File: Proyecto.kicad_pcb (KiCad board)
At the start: 2 copper layers, 42 parts, among them IC1 ATMEGA328P-A, P1 CONN_01X03, P2 CONN_01X03, Q1 BC808-40, Q2 BC808-40, SW1 SW_PUSH, U2 MCP2551-I/SN, U3 AMS1117, U4 ACS712, U5 ACS712

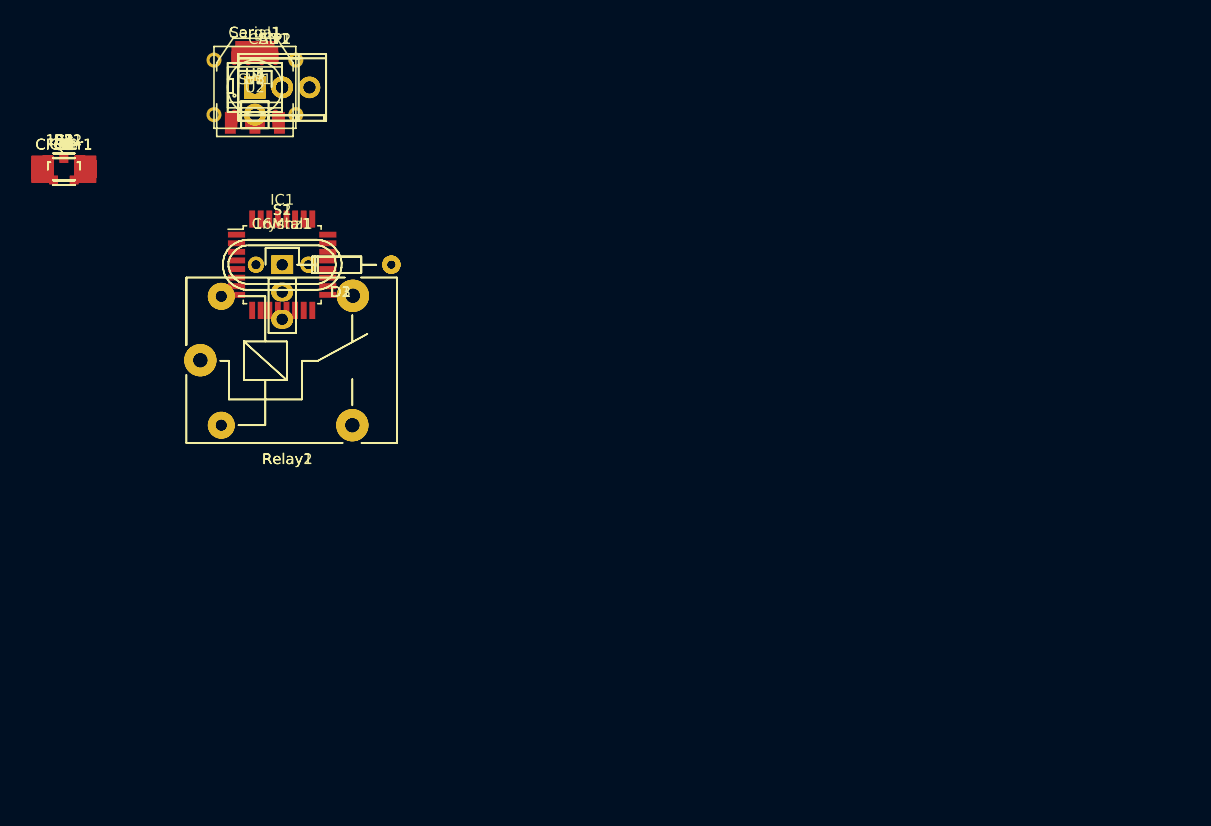
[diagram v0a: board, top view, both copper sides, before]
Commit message: fix
se quito el micro y se coloco pines hembra para insertar NanoArduino en
placa
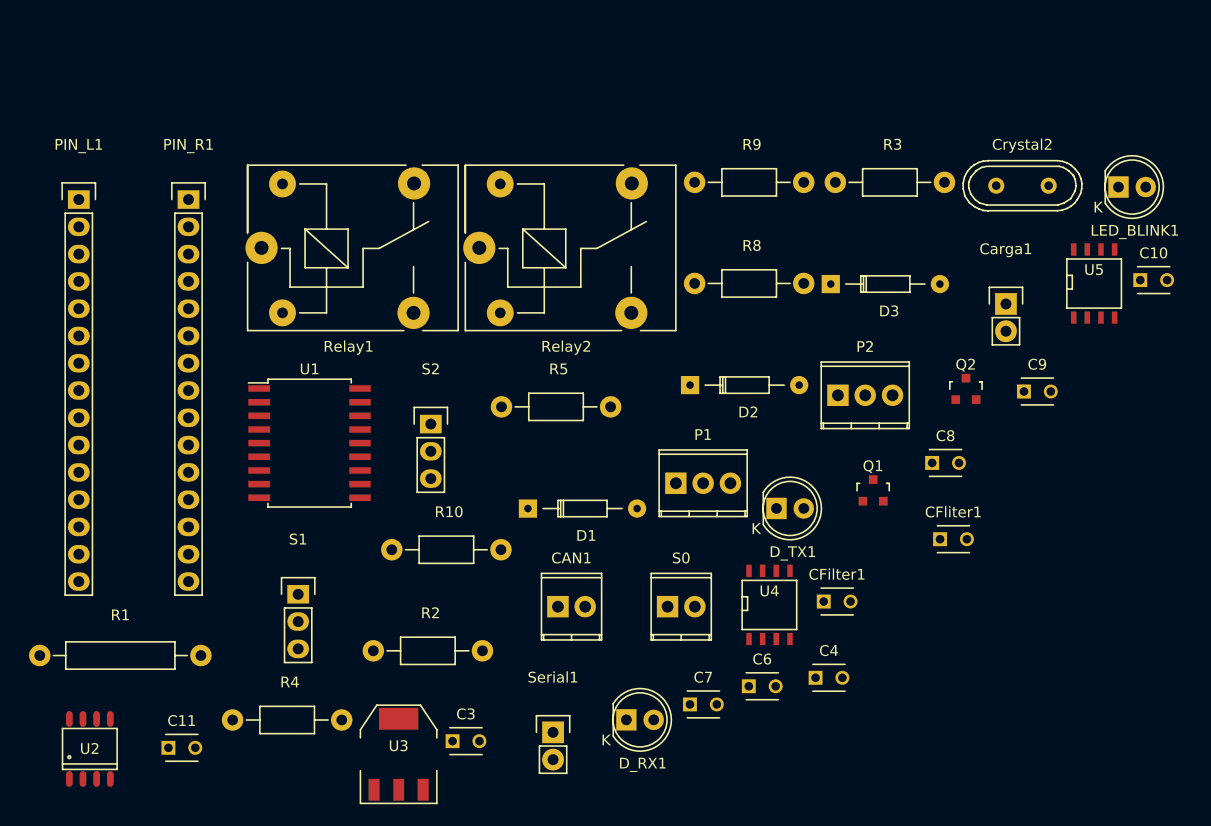
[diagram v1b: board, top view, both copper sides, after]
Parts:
- removed 10k1, 10k2: R, Resistors_SMD:R_1210
- removed 16Mhz1: Crystal, Crystals:Crystal_HC49-U_Vertical
- removed C1, C2: 22pf, Capacitors_SMD:C_1210
- removed C5: 100nf, Capacitors_SMD:C_1206_HandSoldering
- removed Crystal1: 16mhz, Crystals:Crystal_HC49-U_Vertical
- removed IC1: ATMEGA328P-A, Housings_QFP:TQFP-32_7x7mm_Pitch0.8mm
- removed SW1: SW_PUSH, Buttons_Switches_ThroughHole:SW_PUSH_SMALL
- added Crystal2: 16Mhz, Crystals:Crystal_HC49-U_Vertical, F.Cu at (193.3, 65.9)
- added D_RX1: LED, LEDs:LED-5MM, F.Cu at (156.4, 115.6)
- added D_TX1: LED, LEDs:LED-5MM, F.Cu at (170.4, 95.9)
- added LED_BLINK1: LED, LEDs:LED-5MM, F.Cu at (202.2, 66.0)
- added PIN_L1: CONN_01X15, Pin_Headers:Pin_Header_Straight_1x15, F.Cu at (105.4, 67.2)
- added PIN_R1: CONN_01X15, Pin_Headers:Pin_Header_Straight_1x15, F.Cu at (115.6, 67.2)
- added R10: 1k, Resistors_ThroughHole:Resistor_Horizontal_RM10mm, F.Cu at (134.6, 99.8)
- added R5: 120, Resistors_ThroughHole:Resistor_Horizontal_RM10mm, F.Cu at (144.8, 86.5)
- added R8: 1k, Resistors_ThroughHole:Resistor_Horizontal_RM10mm, F.Cu at (162.8, 75.0)
- added R9: 1k, Resistors_ThroughHole:Resistor_Horizontal_RM10mm, F.Cu at (162.8, 65.6)
- added U1: MCP2515, Housings_SOIC:SOIC-18_7.5x11.6mm_Pitch1.27mm, F.Cu at (126.9, 89.9)
- C10, C11, C3, C4, C6, C7, C8, C9: footprint Capacitors_SMD:C_1206_HandSoldering -> Capacitors_ThroughHole:C_Disc_D3_P2.5
- CFilter1, CFliter1: footprint Capacitors_SMD:C_1206 -> Capacitors_ThroughHole:C_Disc_D3_P2.5
- R1: value R -> 10k; footprint Resistors_SMD:R_1206_HandSoldering -> Resistors_ThroughHole:Resistor_Horizontal_RM15mm
- R2: value R -> 10k; footprint Resistors_SMD:R_1210_HandSoldering -> Resistors_ThroughHole:Resistor_Horizontal_RM10mm
- R3: value R -> 1k; footprint Resistors_SMD:R_1210_HandSoldering -> Resistors_ThroughHole:Resistor_Horizontal_RM10mm
- R4: value 120 -> 1k; footprint Resistors_SMD:R_1210_HandSoldering -> Resistors_ThroughHole:Resistor_Horizontal_RM10mm
- moved C10 100.7 mm to (204.3, 74.7)
- moved C9 91.7 mm to (193.4, 85.1)
- moved CFliter1 88.5 mm to (185.6, 98.8)
- moved Q2 86.4 mm to (188.0, 84.8)
- moved C8 85.3 mm to (184.9, 91.7)
- moved C4 84.5 mm to (174.0, 111.7)
- moved CFilter1 81.4 mm to (174.8, 104.6)
- moved Q1 81.0 mm to (179.4, 94.3)
- moved U5 80.2 mm to (200.0, 75.0)
- moved C6 79.9 mm to (167.8, 112.5)
- moved C7 76.7 mm to (162.3, 114.2)
- moved Carga1 72.8 mm to (191.7, 76.9)
- moved R3 71.8 mm to (175.9, 65.6)
- moved U4 67.9 mm to (169.7, 104.9)
- moved Serial1 66.1 mm to (149.6, 116.8)
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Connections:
- R1 pad 2: RESET -> Net-(R1-Pad2)
- R2 pad 1: Net-(Q1-Pad1) -> +5V
- R2 pad 2: Net-(IC1-Pad11) -> /CS
- R3 pad 1: Net-(Q2-Pad1) -> Net-(Q1-Pad1)
- R3 pad 2: Net-(IC1-Pad10) -> /R2
- R4 pad 1: Net-(CAN1-Pad2) -> Net-(Q2-Pad1)
- R4 pad 2: Net-(Carga1-Pad1) -> /R1
- U4 pad 1: Net-(P1-Pad3) -> Net-(Relay1-Pad1)
- U4 pad 2: Net-(P1-Pad3) -> Net-(Relay1-Pad1)
- U4 pad 3: Net-(Relay1-Pad1) -> Net-(P1-Pad3)
- U4 pad 4: Net-(Relay1-Pad1) -> Net-(P1-Pad3)
- U4 pad 7: AC1 -> /AC1
- U5 pad 7: AC2 -> /AC2
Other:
- rule pad_to_mask_clearance: 0.2 -> 0

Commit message: fix pcb
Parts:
- moved CAN1 74.5 mm to (85.1, 68.6)
- moved U4 65.7 mm to (147.3, 43.2)
- moved U5 52.7 mm to (147.3, 72.4), turned to 180 degrees
- moved D_TX1 52.1 mm to (208.5, 131.5)
- moved Q1 52.1 mm to (217.5, 129.8)
- moved C8 52.1 mm to (223.0, 127.3)
- moved CFliter1 52.1 mm to (223.7, 134.4)
- moved Carga1 52.1 mm to (229.8, 112.5)
- moved Crystal2 52.1 mm to (231.4, 101.5)
- moved D3 52.1 mm to (213.5, 110.6)
- moved R3 52.1 mm to (214.0, 101.1)
- moved C9 52.1 mm to (231.5, 120.6)
- moved CFilter1 52.1 mm to (212.9, 140.2)
- moved Q2 52.1 mm to (226.1, 120.4)
- moved P1 47.9 mm to (162.6, 45.7), turned to 270 degrees
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
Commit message: fix terrena
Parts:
- added D4: LED 2, LEDs:LED-5MM, B.Cu at (122.9, 108.7)
- added R11: 1k, Resistors_ThroughHole:Resistor_Horizontal_RM10mm, B.Cu at (117.3, 108.7)
- C10, C11, C4, C8, C9, CAN1, CFilter1, CFliter1, Carga1, Crystal2, D1, D2, D3, D_RX1, D_TX1, LED_BLINK1, P1, P2, R10, R2, R3, R4, R5, R8, R9, Relay1, Relay2, S0: moved to B.Cu
- R1: footprint Resistors_ThroughHole:Resistor_Horizontal_RM15mm -> Resistors_ThroughHole:Resistor_Horizontal_RM10mm; moved to B.Cu
- U2: footprint Power_Integrations:SO-8 -> SMD_Packages:SOIC-8-N
- moved CFliter1 146.4 mm to (98.6, 58.4), turned to 180 degrees
- moved Q2 127.1 mm to (106.2, 78.5), turned to 180 degrees
- moved CFilter1 125.6 mm to (93.5, 101.1), turned to 180 degrees
- moved Q1 116.3 mm to (106.2, 96.3), turned to 90 degrees
- moved C10 116.0 mm to (89.4, 58.4)
- moved D3 113.1 mm to (106.2, 74.9), turned to 90 degrees
- moved R3 99.9 mm to (114.3, 94.0), turned to 90 degrees
- moved P1 95.5 mm to (78.2, 90.6), turned to 90 degrees
- moved CAN1 90.0 mm to (164.3, 111.3)
- moved P2 85.2 mm to (78.2, 74.0), turned to 90 degrees
- moved U2 82.1 mm to (165.2, 98.3), turned to 180 degrees
- moved C8 82.0 mm to (172.7, 62.5)
- moved U1 82.0 mm to (157.2, 66.5), turned to 180 degrees
- moved C9 78.9 mm to (172.7, 68.1)
- moved U4 74.4 mm to (93.5, 94.5), turned to 180 degrees
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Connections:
- LED_BLINK1 pad 2: /LED_BLINK -> /LED
- PIN_L1 pad 1: Net-(PIN_L1-Pad1) -> /SO
- PIN_L1 pad 11: Net-(PIN_L1-Pad11) -> /LED
- PIN_L1 pad 12: /INT -> GND
- PIN_L1 pad 13: /CS -> Net-(PIN_L1-Pad13)
- PIN_L1 pad 14: /SI -> /tx
- PIN_L1 pad 15: /SO -> /rx
- PIN_L1 pad 2: Net-(PIN_L1-Pad2) -> /SI
- PIN_L1 pad 3: Net-(PIN_L1-Pad3) -> /CS
- PIN_L1 pad 4: GND -> /INT
- PIN_L1 pad 5: /LED_BLINK -> Net-(PIN_L1-Pad5)
- PIN_R1 pad 12: Net-(PIN_R1-Pad12) -> +5V
- Relay1 pad 3: Net-(P1-Pad2) -> Net-(P1-Pad1)
- Relay1 pad 4: Net-(P1-Pad1) -> Net-(P1-Pad3)
- Relay2 pad 3: Net-(P2-Pad2) -> Net-(P2-Pad1)
- Relay2 pad 4: Net-(P2-Pad1) -> Net-(P2-Pad3)
- S1 pad 2: GND -> +5V
- S1 pad 3: +5V -> GND
- S2 pad 2: GND -> +5V
- S2 pad 3: +5V -> GND
- Serial1 pad 1: Net-(PIN_L1-Pad2) -> /rx
- Serial1 pad 2: Net-(PIN_L1-Pad1) -> /tx
- U2 pad 6: Net-(CAN1-Pad2) -> Net-(CAN1-Pad1)
- U2 pad 7: Net-(CAN1-Pad1) -> Net-(CAN1-Pad2)
- U3 pad 4: (no net) -> +5V
- U4 pad 3: Net-(P1-Pad3) -> Net-(P1-Pad2)
- U4 pad 4: Net-(P1-Pad3) -> Net-(P1-Pad2)
- U5 pad 1: Net-(P2-Pad3) -> Net-(P2-Pad2)
- U5 pad 2: Net-(P2-Pad3) -> Net-(P2-Pad2)
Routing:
- net GND: track 0.00 -> 271.6 mm
- net +5V: track 0.00 -> 207.0 mm
- net Net-(R9-Pad2): track 0.00 -> 64.0 mm
- net /SCK: track 0.00 -> 45.1 mm
- net /INT: track 0.00 -> 39.9 mm
- net Net-(R8-Pad2): track 0.00 -> 31.5 mm
- net Net-(C6-Pad1): track 0.00 -> 24.1 mm
- net Net-(CAN1-Pad1): track 0.00 -> 18.5 mm
- net /SO: track 0.00 -> 17.4 mm, vias 0 -> 2
- net pin23: track 0.00 -> 16.6 mm
- net Net-(P2-Pad2): track 0.00 -> 16.5 mm
- net Net-(P1-Pad2): track 0.00 -> 16.0 mm
- net /SI: track 0.00 -> 14.9 mm
- net /CS: track 0.00 -> 14.5 mm
- net Net-(LED_BLINK1-Pad1): track 0.00 -> 13.7 mm
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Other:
- board outline added: 102.6 x 58.9 mm
- net class Default: clearance 0.2 -> 0.3556; trace_width 0.25 -> 0.3048; via_dia 0.6 -> 1.2; via_drill 0.4 -> 0.8
- rule trace_clearance: 0.2 -> 0.3556
- rule trace_min: 0.2 -> 0.3048
- rule via_min_drill: 0.3 -> 0.8
- rule via_min_size: 0.4 -> 1.2

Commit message: fix
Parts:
- PIN_L1, PIN_R1, S1, S2: moved to B.Cu
- moved R1 116.1 mm to (34.6, 105.5)
- moved R2 116.1 mm to (30.5, 103.0)
- moved C4 111.7 mm to (61.6, 132.3)
- moved R8 110.3 mm to (58.6, 127.3)
- moved R9 110.3 mm to (58.6, 117.6)
- moved D_TX1 110.3 mm to (53.5, 127.0)
- moved Serial1 110.3 mm to (41.3, 140.0)
- moved U2 110.3 mm to (62.8, 139.2)
- moved R5 110.3 mm to (64.7, 146.6)
- moved CAN1 110.3 mm to (61.9, 152.1)
- moved Carga1 110.3 mm to (55.0, 142.0)
- moved D_RX1 110.3 mm to (53.5, 119.4)
- moved S0 110.3 mm to (53.5, 152.1)
- moved R10 109.1 mm to (56.3, 133.1), turned to 90 degrees
- moved LED_BLINK1 109.0 mm to (47.4, 132.3)
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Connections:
- PIN_L1 pad 12: GND -> Net-(PIN_L1-Pad12)
- Relay1 pad 2: +5V -> Net-(D2-Pad2)
- Relay1 pad 5: Net-(D2-Pad2) -> +5V
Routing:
- net GND: track 271.6 -> 0.00 mm
- net +5V: track 207.0 -> 3.06 mm
- net Net-(R9-Pad2): track 64.0 -> 1.52 mm
- net /INT: track 39.9 -> 7.81 mm
- net Net-(R8-Pad2): track 31.5 -> 0.00 mm
- net Net-(C6-Pad1): track 24.1 -> 0.36 mm
- net Net-(CAN1-Pad1): track 18.5 -> 0.00 mm
- net pin23: track 16.6 -> 0.00 mm
- net Net-(P2-Pad2): track 16.5 -> 0.00 mm
- net Net-(P1-Pad2): track 16.0 -> 0.00 mm
- net Net-(LED_BLINK1-Pad1): track 13.7 -> 0.00 mm
- net Net-(Q2-Pad1): track 12.9 -> 0.00 mm
- net Net-(C9-Pad1): track 12.5 -> 0.50 mm
- net /R2: track 11.2 -> 0.00 mm
- net pin24: track 11.1 -> 0.00 mm
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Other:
- board outline removed
- net class Default: clearance 0.3556 -> 0.55
- rule trace_clearance: 0.3556 -> 0.55

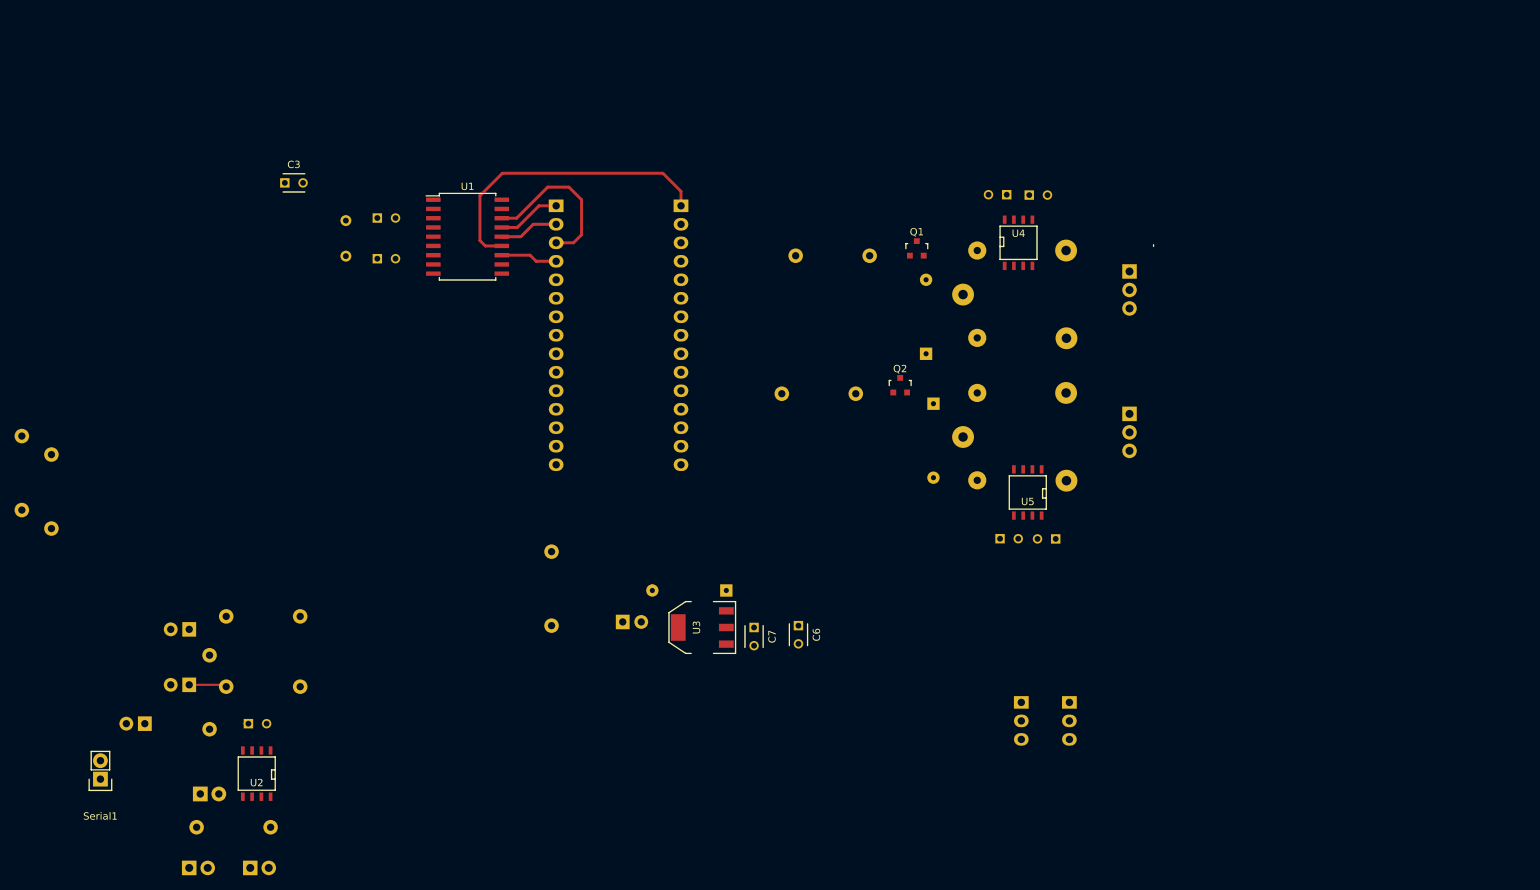
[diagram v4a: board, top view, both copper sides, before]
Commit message: fix casa
se dieron vuelta los pines del nano arudino
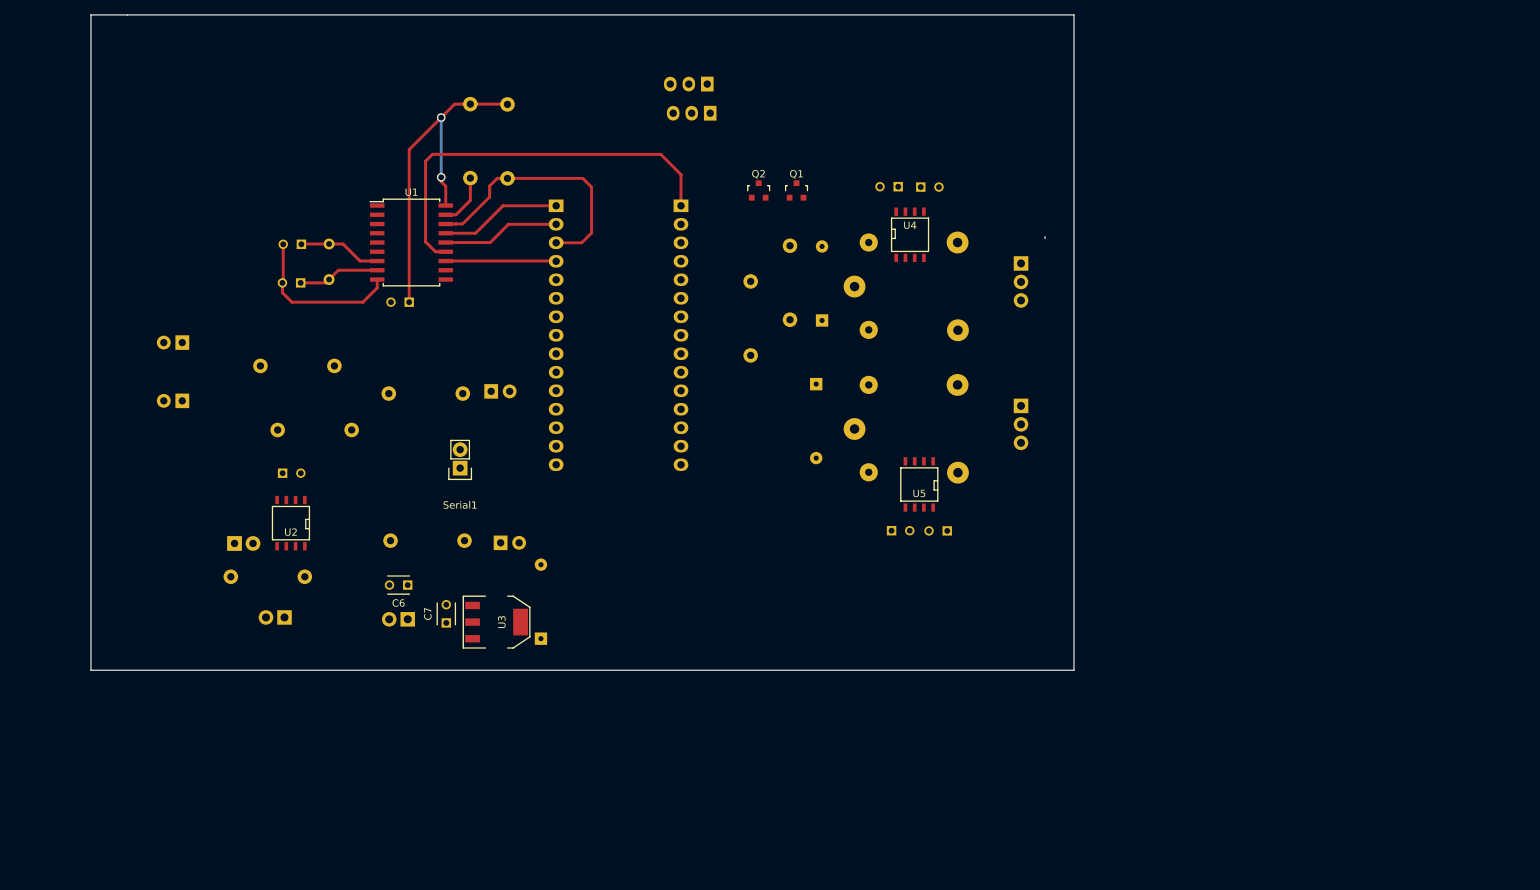
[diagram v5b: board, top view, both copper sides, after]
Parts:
- C3: moved to B.Cu
- moved S2 98.4 mm to (124.6, 44.5), turned to 90 degrees
- moved S1 91.5 mm to (125.0, 48.5), turned to 90 degrees
- moved R2 86.9 mm to (97.2, 47.3), turned to 270 degrees
- moved R1 81.9 mm to (92.1, 47.2), turned to 270 degrees
- moved LED_BLINK1 65.9 mm to (95.0, 86.7), turned to 0 degrees
- moved Serial1 65.3 mm to (90.7, 97.2)
- moved R10 57.7 mm to (91.1, 87.0), turned to 180 degrees
- moved C6 53.9 mm to (83.5, 113.3), turned to 180 degrees
- moved S0 45.5 mm to (83.5, 118.0), turned to 180 degrees
- moved C7 42.3 mm to (88.8, 118.5), turned to 90 degrees
- moved D_RX1 39.4 mm to (52.5, 80.0)
- moved D_TX1 39.0 mm to (52.5, 88.0)
- moved R8 36.0 mm to (65.6, 92.0)
- moved C4 34.7 mm to (66.3, 97.9)
- moved R9 34.7 mm to (63.3, 83.2)
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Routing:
- net (no net): track 0.00 -> 141.5 mm
- net +5V: track 3.06 -> 49.9 mm, vias 0 -> 2
- net GND: track 0.00 -> 22.2 mm
- net /CS: track 22.2 -> 37.1 mm
- net /SCK: track 41.4 -> 55.3 mm
- net Net-(C9-Pad1): track 0.50 -> 11.4 mm
- net Net-(C8-Pad1): track 0.64 -> 11.2 mm
- net /SI: track 8.17 -> 16.2 mm
- net /SO: track 8.70 -> 16.7 mm
- net /INT: track 7.81 -> 15.2 mm
- net Net-(R1-Pad2): track 0.00 -> 7.26 mm
- net Net-(D_TX1-Pad1): track 5.19 -> 0.00 mm
- net /LED: track 0.76 -> 0.00 mm
- net Net-(D3-Pad2): track 0.51 -> 0.00 mm
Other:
- board outline added: 135 x 90 mm

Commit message: fix terrena
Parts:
- removed D4: LED 2, LEDs:LED-5MM
- removed LED_BLINK1: LED, LEDs:LED-5MM
- removed Serial1: CONN_01X02, Pin_Headers:Pin_Header_Straight_1x02
- added ESP8266: CONN_02X04, Pin_Headers:Pin_Header_Straight_2x04, B.Cu at (112.9, 108.1)
- added LED1: LED, LEDs:LED-5MM, B.Cu at (90.8, 82.0)
- added LED_Gp1: LED, LEDs:LED-5MM, B.Cu at (105.7, 115.3)
- added LED_Gp2: LED, LEDs:LED-5MM, B.Cu at (112.4, 115.6)
- added LED_Vcc1: LED, LEDs:LED-5MM, B.Cu at (84.3, 97.0)
- added R12: 1k, Resistors_ThroughHole:Resistor_Horizontal_RM10mm, B.Cu at (104.1, 101.6)
- added R13: 2k2, Resistors_ThroughHole:Resistor_Horizontal_RM10mm, B.Cu at (118.4, 101.6)
- added R6: 1k, Resistors_ThroughHole:Resistor_Horizontal_RM10mm, B.Cu at (122.6, 115.6)
- added R7: 1k, Resistors_ThroughHole:Resistor_Horizontal_RM10mm, B.Cu at (127.0, 115.6)
- C6, C7: moved to B.Cu
- moved C10 97.4 mm to (63.9, 79.4), turned to 270 degrees
- moved C4 91.5 mm to (148.8, 58.4)
- moved C3 81.2 mm to (158.5, 106.2)
- moved C11 67.5 mm to (85.3, 74.7)
- moved D_TX1 41.0 mm to (78.3, 56.1), turned to 0 degrees
- moved R8 40.1 mm to (73.8, 52.7), turned to 270 degrees
- moved D_RX1 40.1 mm to (78.4, 49.4), turned to 0 degrees
- moved R9 33.7 mm to (67.6, 49.8), turned to 270 degrees
- moved R5 23.5 mm to (65.8, 88.9), turned to 0 degrees
- moved U2 22.7 mm to (69.8, 82.3)
- moved CAN1 22.1 mm to (64.6, 95.8), turned to 90 degrees
- moved S0 20.7 mm to (65.5, 107.7), turned to 90 degrees
- moved C7 19.4 mm to (74.7, 105.2)
- moved U3 19.4 mm to (81.6, 105.1)
- moved D1 14.7 mm to (91.4, 110.2)
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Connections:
- PIN_L1 pad 12: Net-(PIN_L1-Pad12) -> GND
- PIN_L1 pad 14: /tx -> Net-(ESP8266-Pad7)
- PIN_L1 pad 15: /rx -> Net-(PIN_L1-Pad15)
- PIN_R1 pad 10: /R2 -> /AC2
- PIN_R1 pad 2: Net-(PIN_R1-Pad2) -> /3.3V
- PIN_R1 pad 8: /AC2 -> /AC1
- PIN_R1 pad 9: /AC1 -> /R2
- S0 pad 1: Net-(C6-Pad1) -> Net-(S0-Pad1)
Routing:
- net GND: track 22.2 -> 422.4 mm, vias 0 -> 5
- net +5V: track 49.9 -> 421.4 mm, vias 2 -> 4
- net (no net): track 141.5 -> 0.00 mm
- net /AC1: track 0.00 -> 53.1 mm
- net Net-(D3-Pad2): track 0.00 -> 49.2 mm
- net /AC2: track 0.00 -> 43.2 mm
- net Net-(R9-Pad2): track 1.52 -> 43.0 mm
- net Net-(R8-Pad2): track 0.00 -> 32.9 mm
- net pin23: track 0.00 -> 32.4 mm
- net Net-(C6-Pad1): track 0.00 -> 27.4 mm
- net Net-(LED_Gp1-Pad1): track 0.00 -> 27.0 mm
- net pin24: track 0.00 -> 26.8 mm
- net Net-(CAN1-Pad1): track 0.00 -> 25.7 mm
- net Net-(ESP8266-Pad7): track 0.00 -> 23.3 mm
- net Net-(Q2-Pad1): track 0.00 -> 20.4 mm
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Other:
- board size 135 x 90 mm -> 111.1 x 84.8 mm
